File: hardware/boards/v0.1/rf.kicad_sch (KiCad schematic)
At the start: 7 parts, among them U22 nRF, Y2 32.768kHz

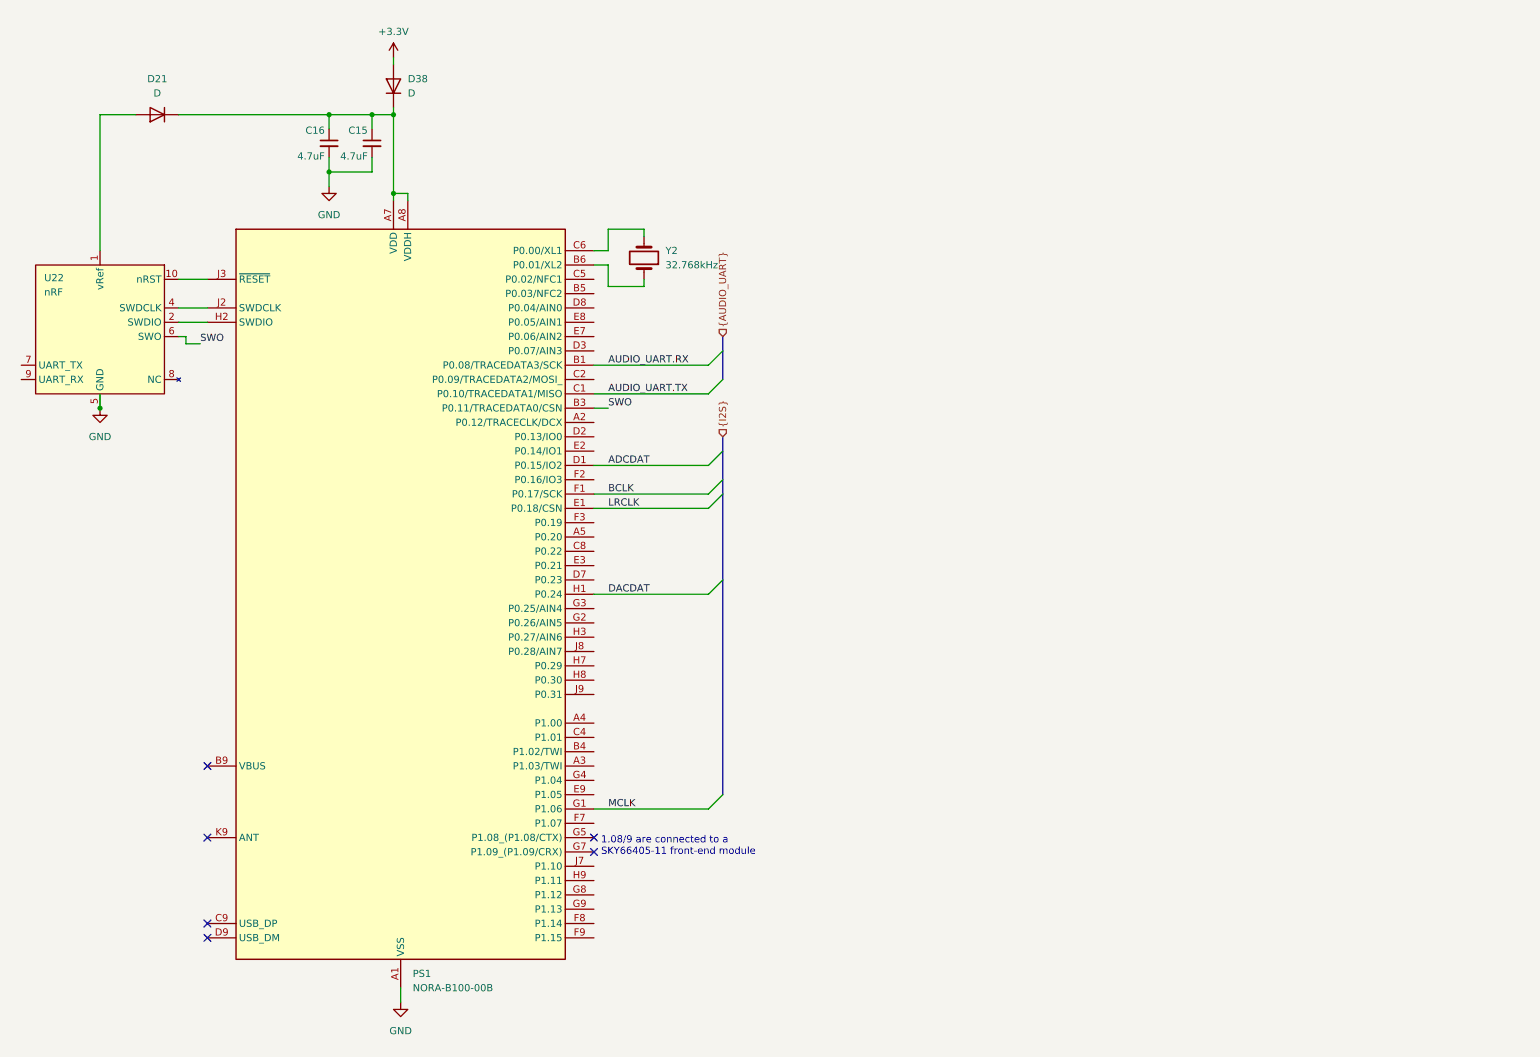
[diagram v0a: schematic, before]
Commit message: feat: various component and layout changes
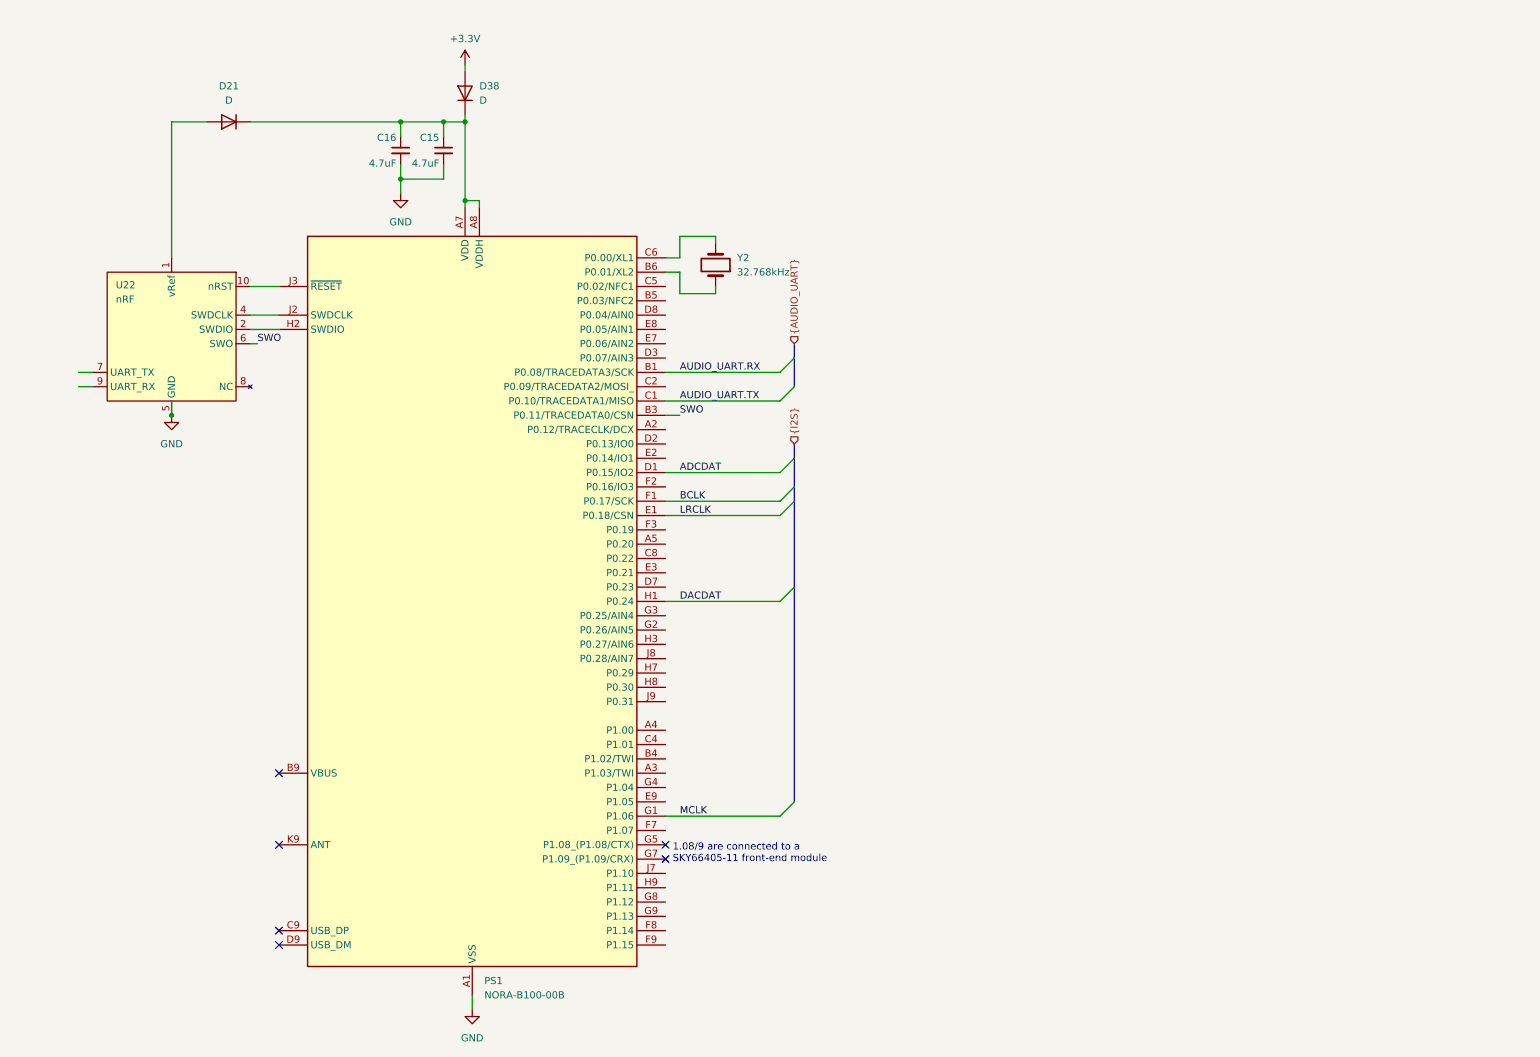
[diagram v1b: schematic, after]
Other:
- moved on the sheet: C15, C16, D21, D38, PS1, U22, Y2

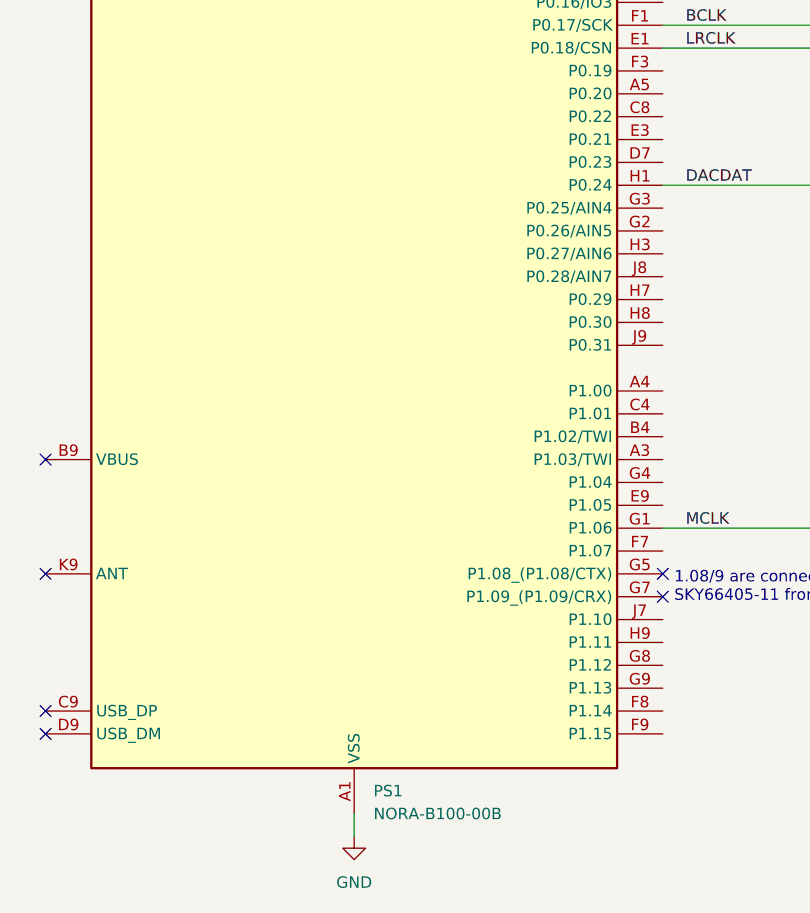
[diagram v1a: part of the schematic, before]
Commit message: feat: schematic organization
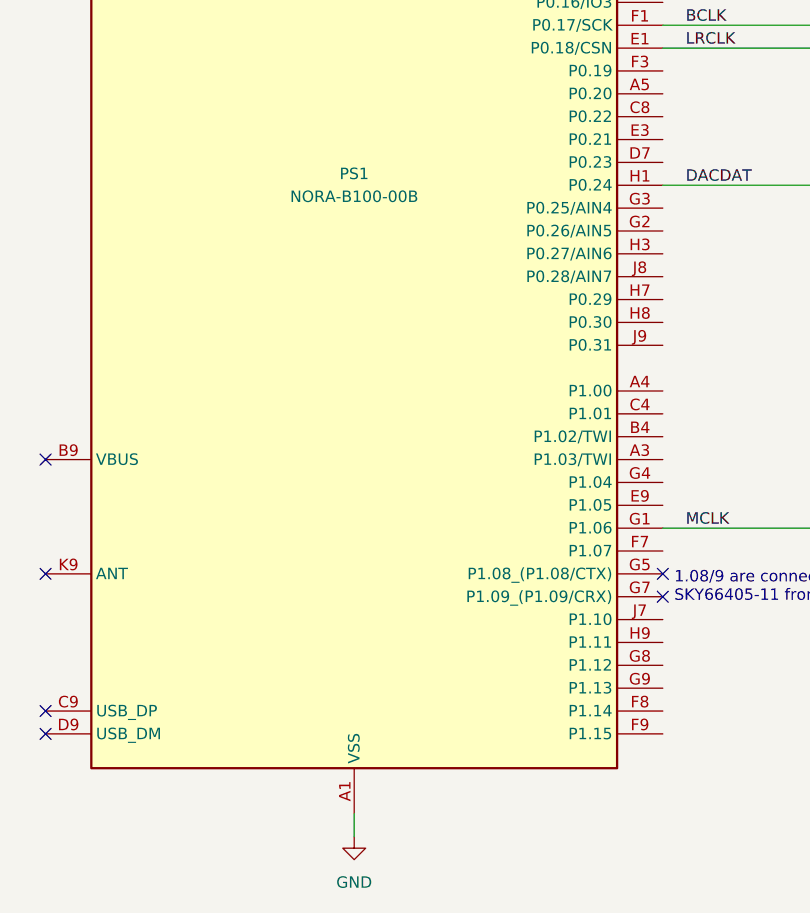
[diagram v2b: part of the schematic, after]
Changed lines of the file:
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@@
 		(on_board yes)
 		(dnp no)
-		(fields_autoplaced yes)
 		(property "Reference" "PS1"
-			(at 97.3933 184.15 0)
+			(at 95.25 115.57 0)
 			(effects
 				(font
 					(size 1.27 1.27)
 				)
-				(justify left)
 			)
 		)
 		(property "Value" "NORA-B100-00B"
-			(at 97.3933 186.69 0)
+			(at 95.25 118.11 0)
 			(effects
 				(font
 					(size 1.27 1.27)
 				)
-				(justify left)
 			)
 		)

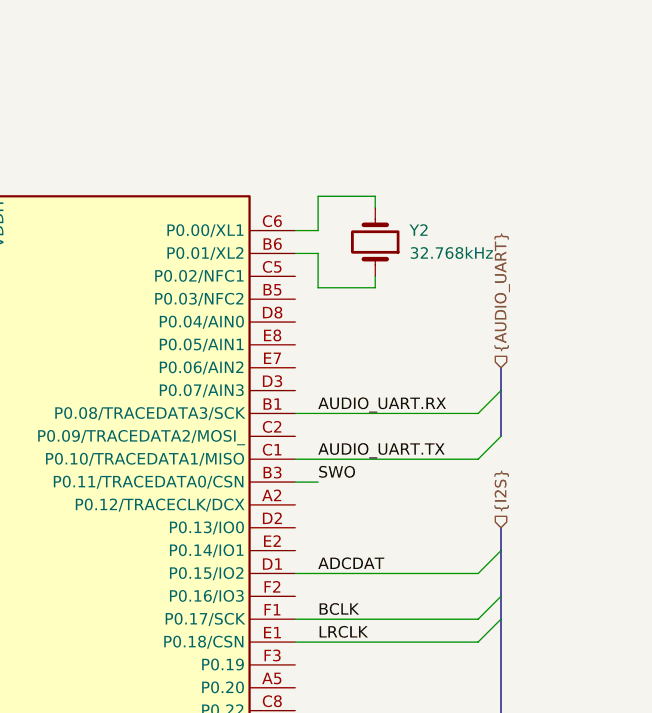
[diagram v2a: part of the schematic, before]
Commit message: feat: schematic organization, MIDI port routing
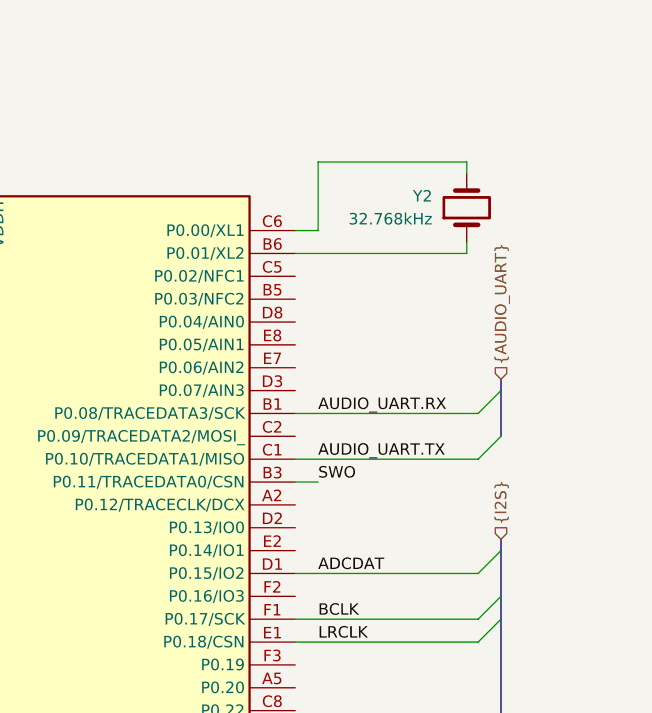
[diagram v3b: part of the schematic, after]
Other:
- moved on the sheet: Y2
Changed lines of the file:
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@@
+		)
+	)
+	(wire
+		(pts
+			(xy 129.54 58.42) (xy 148.59 58.42)
+		)
+		(stroke
+			(width 0)
+			(type default)
 		)
 	)
@@
 	(bus
 		(pts
-			(xy 152.4 71.12) (xy 152.4 73.66)
-		)
-		(stroke
-			(width 0)
-			(type default)
-		)
-	)
-	(wire
-		(pts
-			(xy 138.43 62.23) (xy 138.43 60.96)
+			(xy 152.4 72.39) (xy 152.4 73.66)
+		)
+		(stroke
+			(width 0)
+			(type default)
+		)
+	)
+	(wire
+		(pts
+			(xy 148.59 58.42) (xy 148.59 57.15)
 		)
 		(stroke
@@
 	(wire
 		(pts
-			(xy 132.08 62.23) (xy 138.43 62.23)
-		)
-		(stroke
-			(width 0)
-			(type default)
-		)
-	)
-	(wire
-		(pts
 			(xy 95.25 186.69) (xy 95.25 189.23)
 		)
@@
 	(wire
 		(pts
-			(xy 132.08 62.23) (xy 132.08 58.42)
-		)
-		(stroke
-			(width 0)
-			(type default)
-		)
-	)
-	(wire
-		(pts
 			(xy 55.88 66.04) (xy 60.96 66.04)
 		)
@@
 	(bus
 		(pts
-			(xy 152.4 88.9) (xy 152.4 91.44)
+			(xy 152.4 90.17) (xy 152.4 91.44)
 		)
 		(stroke
@@
 	(wire
 		(pts
-			(xy 132.08 52.07) (xy 138.43 52.07)
+			(xy 132.08 48.26) (xy 148.59 48.26)
 		)
 		(stroke
@@
 	(wire
 		(pts
-			(xy 138.43 52.07) (xy 138.43 53.34)
+			(xy 148.59 48.26) (xy 148.59 49.53)
 		)
 		(stroke
@@
 	(wire
 		(pts
-			(xy 132.08 52.07) (xy 132.08 55.88)
+			(xy 132.08 48.26) (xy 132.08 55.88)
 		)
 		(stroke
@@
 		(pts
 			(xy 57.15 71.12) (xy 55.88 71.12)
-		)
-		(stroke
-			(width 0)
-			(type default)
-		)
-	)
-	(wire
-		(pts
-			(xy 132.08 58.42) (xy 129.54 58.42)
 		)
 		(stroke
@@
 	(hierarchical_label "{AUDIO_UART}"
 		(shape input)
-		(at 152.4 71.12 90)
+		(at 152.4 72.39 90)
 		(effects
 			(font
@@
 	(hierarchical_label "{I2S}"
 		(shape input)
-		(at 152.4 88.9 90)
+		(at 152.4 90.17 90)
 		(effects
 			(font
@@
 			)
 		)
+		(property "Connector" ""
+			(at 52.07 31.75 0)
+			(effects
+				(font
+					(size 1.27 1.27)
+				)
+			)
+		)
 		(pin "1"
 		)
@@
 		)
 		(property "STANDARD" ""
+			(at 82.55 36.83 0)
+			(effects
+				(font
+					(size 1.27 1.27)
+				)
+			)
+		)
+		(property "Connector" ""
 			(at 82.55 36.83 0)
 			(effects
@@
 			)
 		)
+		(property "Connector" ""
+			(at 90.17 36.83 0)
+			(effects
+				(font
+					(size 1.27 1.27)
+				)
+			)
+		)
 		(pin "1"
 		)
@@
 			)
 		)
+		(property "Connector" ""
+			(at 93.98 26.67 0)
+			(effects
+				(font
+					(size 1.27 1.27)
+				)
+			)
+		)
 		(pin "1"
 		)
@@
 			)
 		)
+		(property "Connector" ""
+			(at 95.25 116.84 0)
+			(effects
+				(font
+					(size 1.27 1.27)
+				)
+			)
+		)
 		(pin "J2"
 		)
@@
 	(symbol
 		(lib_id "Device:Crystal")
-		(at 138.43 57.15 270)
-		(mirror x)
+		(at 148.59 53.34 90)
 		(unit 1)
 		(exclude_from_sim no)
@@
 		(dnp no)
 		(property "Reference" "Y2"
-			(at 142.24 55.8799 90)
+			(at 144.78 52.0699 90)
 			(effects
 				(font
@@
 		)
 		(property "Value" "32.768kHz"
-			(at 142.24 58.4199 90)
+			(at 144.78 54.6099 90)
 			(effects
 				(font
@@
 		)
 		(property "Footprint" ""
-			(at 138.43 57.15 0)
+			(at 148.59 53.34 0)
 			(effects
 				(font
@@
 		)
 		(property "Datasheet" "~"
-			(at 138.43 57.15 0)
+			(at 148.59 53.34 0)
 			(effects
 				(font
@@
 		)
 		(property "Description" "Two pin crystal"
-			(at 138.43 57.15 0)
+			(at 148.59 53.34 0)
 			(effects
 				(font
@@
 		)
 		(property "Arrow Part Number" ""
-			(at 138.43 57.15 0)
+			(at 148.59 53.34 0)
 			(effects
 				(font
@@
 		)
 		(property "Arrow Price/Stock" ""
-			(at 138.43 57.15 0)
+			(at 148.59 53.34 0)
 			(effects
 				(font
@@
 		)
 		(property "MANUFACTURER" ""
-			(at 138.43 57.15 0)
+			(at 148.59 53.34 0)
 			(effects
 				(font
@@
 		)
 		(property "MAXIMUM_PACKAGE_HEIGHT" ""
-			(at 138.43 57.15 0)
+			(at 148.59 53.34 0)
 			(effects
 				(font
@@
 		)
 		(property "PARTREV" ""
-			(at 138.43 57.15 0)
+			(at 148.59 53.34 0)
 			(effects
 				(font
@@
 		)
 		(property "STANDARD" ""
-			(at 138.43 57.15 0)
+			(at 148.59 53.34 0)
+			(effects
+				(font
+					(size 1.27 1.27)
+				)
+			)
+		)
+		(property "Connector" ""
+			(at 148.59 53.34 0)
 			(effects
 				(font
@@
 			(at 41.91 69.85 0)
 			(effects
+				(font
+					(size 1.27 1.27)
+				)
+			)
+		)
+		(property "Connector" ""
+			(at 41.91 69.85 0)
+			(effects

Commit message: feat: start adding Wifi module
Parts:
- added U27: ESP32-S3-MINI-1U, RF_Module:ESP32-S2-MINI-1U, symbol RF_Module:ESP32-S3-MINI-1U
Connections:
- new net: U27.1 (GND), U27.2 (GND), U27.42 (GND), U27.43 (GND), U27.46 (GND), U27.47 (GND), U27.48 (GND), U27.49 (GND), U27.50 (GND), U27.51 (GND), U27.52 (GND), U27.53 (GND), U27.54 (GND), U27.55 (GND), U27.56 (GND), U27.57 (GND), U27.58 (GND), U27.59 (GND), U27.60 (GND), U27.61 (GND), U27.62 (GND), U27.63 (GND), U27.64 (GND), U27.65 (GND)
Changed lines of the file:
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@@
+	)
+	(symbol
+		(lib_id "RF_Module:ESP32-S3-MINI-1U")
+		(at 207.01 74.93 0)
+		(unit 1)
+		(exclude_from_sim no)
+		(in_bom yes)
+		(on_board yes)
+		(dnp no)
+		(fields_autoplaced yes)
+		(property "Reference" "U27"
+			(at 209.1533 41.91 0)
+			(effects
+				(font
+					(size 1.27 1.27)
+				)
+				(justify left)
+			)
+		)
+		(property "Value" "ESP32-S3-MINI-1U"
+			(at 209.1533 44.45 0)
+			(effects
+				(font
+					(size 1.27 1.27)
+				)
+				(justify left)
+			)
+		)
+		(property "Footprint" "RF_Module:ESP32-S2-MINI-1U"
+			(at 223.52 104.14 0)
+			(effects
+				(font
+					(size 1.27 1.27)
+				)
+				(hide yes)
+			)
+		)
+		(property "Datasheet" "https://www.espressif.com/sites/default/files/documentation/esp32-s3-mini-1_mini-1u_datasheet_en.pdf"
+			(at 207.01 34.29 0)
+			(effects
+				(font
+					(size 1.27 1.27)
+				)
+				(hide yes)
+			)
+		)
+		(property "Description" "RF Module, ESP32-S3 SoC, Wi-Fi 802.11b/g/n, Bluetooth, BLE, 32-bit, 3.3V, SMD, external antenna"
+			(at 207.01 31.75 0)
+			(effects
+				(font
+					(size 1.27 1.27)
+				)
+				(hide yes)
+			)
+		)
+		(pin "21"
+		)
+		(pin "18"
+		)
+		(pin "17"
+		)
+		(pin "48"
+		)
+		(pin "47"
+		)
+		(pin "22"
+		)
+		(pin "60"
+		)
+		(pin "6"
+		)
+		(pin "3"
+		)
+		(pin "5"
+		)
+		(pin "9"
+		)
+		(pin "63"
+		)
+		(pin "64"
+		)
+		(pin "15"
+		)
+		(pin "51"
+		)
+		(pin "42"
+		)
+		(pin "2"
+		)
+		(pin "10"
+		)
+		(pin "7"
+		)
+		(pin "43"
+		)
+		(pin "56"
+		)
+		(pin "45"
+		)
+		(pin "1"
+		)
+		(pin "14"
+		)
+		(pin "61"
+		)
+		(pin "62"
+		)
+		(pin "13"
+		)
+		(pin "12"
+		)
+		(pin "4"
+		)
+		(pin "8"
+		)
+		(pin "46"
+		)
+		(pin "11"
+		)
+		(pin "49"
+		)
+		(pin "52"
+		)
+		(pin "50"
+		)
+		(pin "16"
+		)
+		(pin "55"
+		)
+		(pin "54"
+		)
+		(pin "58"
+		)
+		(pin "57"
+		)
+		(pin "59"
+		)
+		(pin "53"
+		)
+		(pin "20"
+		)
+		(pin "19"
+		)
+		(pin "65"
+		)
+		(pin "39"
+		)
+		(pin "40"
+		)
+		(pin "23"
+		)
+		(pin "24"
+		)
+		(pin "25"
+		)
+		(pin "26"
+		)
+		(pin "28"
+		)
+		(pin "29"
+		)
+		(pin "31"
+		)
+		(pin "32"
+		)
+		(pin "33"
+		)
+		(pin "34"
+		)
+		(pin "35"
+		)
+		(pin "36"
+		)
+		(pin "37"
+		)
+		(pin "38"
+		)
+		(pin "41"
+		)
+		(pin "44"
+		)
+		(pin "27"
+		)
+		(pin "30"
+		)
+		(instances
+			(project ""
+				(path "/485383b8-00f4-4405-b270-de249939cff4/7e9f39e0-07aa-49bf-8354-e1f007de5af0"
+					(reference "U27")
+					(unit 1)
+				)
+			)
+		)
 	)
 	(symbol
